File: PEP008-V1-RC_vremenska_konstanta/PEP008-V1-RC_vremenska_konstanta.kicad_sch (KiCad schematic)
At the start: 23 parts, among them J1 Screw_Terminal_01x02

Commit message: 3, 4, 8.
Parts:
- removed D1, D2: LED, LED_SMD:LED_1206_3216Metric_Pad1.42x1.75mm_HandSolder, symbol Device:LED
- removed J1: Screw_Terminal_01x02, TerminalBlock_Phoenix:TerminalBlock_Phoenix_MKDS-1,5-2-5.08_1x02_P5.08mm_Horizontal, symbol Connector:Screw_Terminal_01x02
- removed JP1, JP2, JP3, JP4, JP5, JP6, JP7, JP8: Jumper, Connector_PinHeader_2.54mm:PinHeader_1x02_P2.54mm_Vertical, symbol Jumper:Jumper_2_Bridged
- removed R2: ~, Resistor_SMD:R_1206_3216Metric_Pad1.30x1.75mm_HandSolder, symbol Device:R
- removed R7: 470, Resistor_SMD:R_1206_3216Metric_Pad1.30x1.75mm_HandSolder, symbol Device:R
- removed R8: 4.7k, Resistor_SMD:R_1206_3216Metric_Pad1.30x1.75mm_HandSolder, symbol Device:R
- added C1, C2: 100u, Capacitor_THT:CP_Radial_D8.0mm_P3.50mm, symbol Device:C_Polarized_US
- added J1, J3, J4, J5: Conn_01x01_Pin, Connector_PinHeader_2.54mm:PinHeader_1x01_P2.54mm_Vertical, symbol Connector:Conn_01x01_Pin
- added J2: Screw_Terminal_01x02, TerminalBlock_Phoenix:TerminalBlock_Phoenix_MKDS-1,5-2-5.08_1x02_P5.08mm_Horizontal, symbol Connector:Screw_Terminal_01x02
- added J6, J7: Conn_01x03_Pin, symbol Connector:Conn_01x03_Pin
- added SW1, SW2: SW_SPDT, Button_Switch_THT:SW_E-Switch_EG1224_SPDT_Angled, symbol Switch:SW_SPDT
- R1: value 470 -> 100k
- R3: value 4.7k -> 10k
- R4: value 47k -> 20k
- R5: value 4.7k -> 50k
- R6: value 470 -> 50k
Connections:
- net 0: now also C2.1, J2.2 (Pin_2), J4.1 (Pin_1), SW2.1 (A)
- net at R3.1: now also J7.3 (Pin_3)
- net at R4.1: now also J7.1 (Pin_1); no longer R3.2
- net Output voltage: now reaches R4.2
- net Output voltage: now also R1.2, R3.2, R5.2, R6.2, C1.1, J1.1 (Pin_1)
- net at R5.1: no longer R6.2
- net at R6.1: now also J6.3 (Pin_3)
- net 9V: no longer names the net of R1.1
- net 9V: now also J6.1 (Pin_1)
- new net: J3.1 (Pin_1), J7.2 (Pin_2), SW2.2 (B)
- new net: J5.1 (Pin_1), J6.2 (Pin_2), SW1.1 (A)
- new net: C1.2, C2.2
- new net Input voltage: J2.1 (Pin_1), SW1.2 (B)
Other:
- note added: "Kondenzator"
- note added: "Putanja za pražnjenje"
- note added: "Putanja za punjenje"
- note removed: "Paralelna otpornost"
- note removed: "Redna otpornost"
- title: Redna i paralelna otpornost -> Punjenje i praznjenje kondenzatora
- moved on the sheet: H1, H2, H3, H4

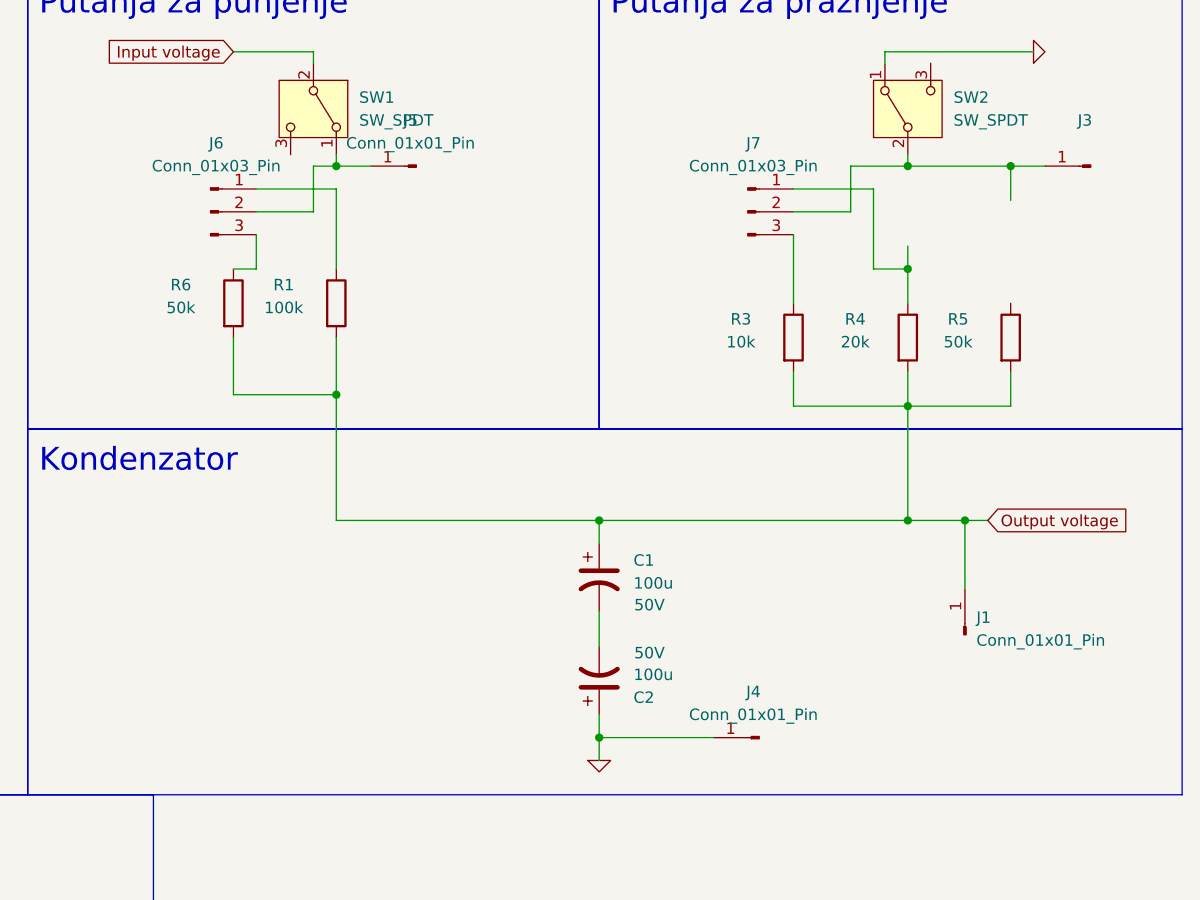
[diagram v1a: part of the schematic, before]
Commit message: PEP006 and PEP009 update.
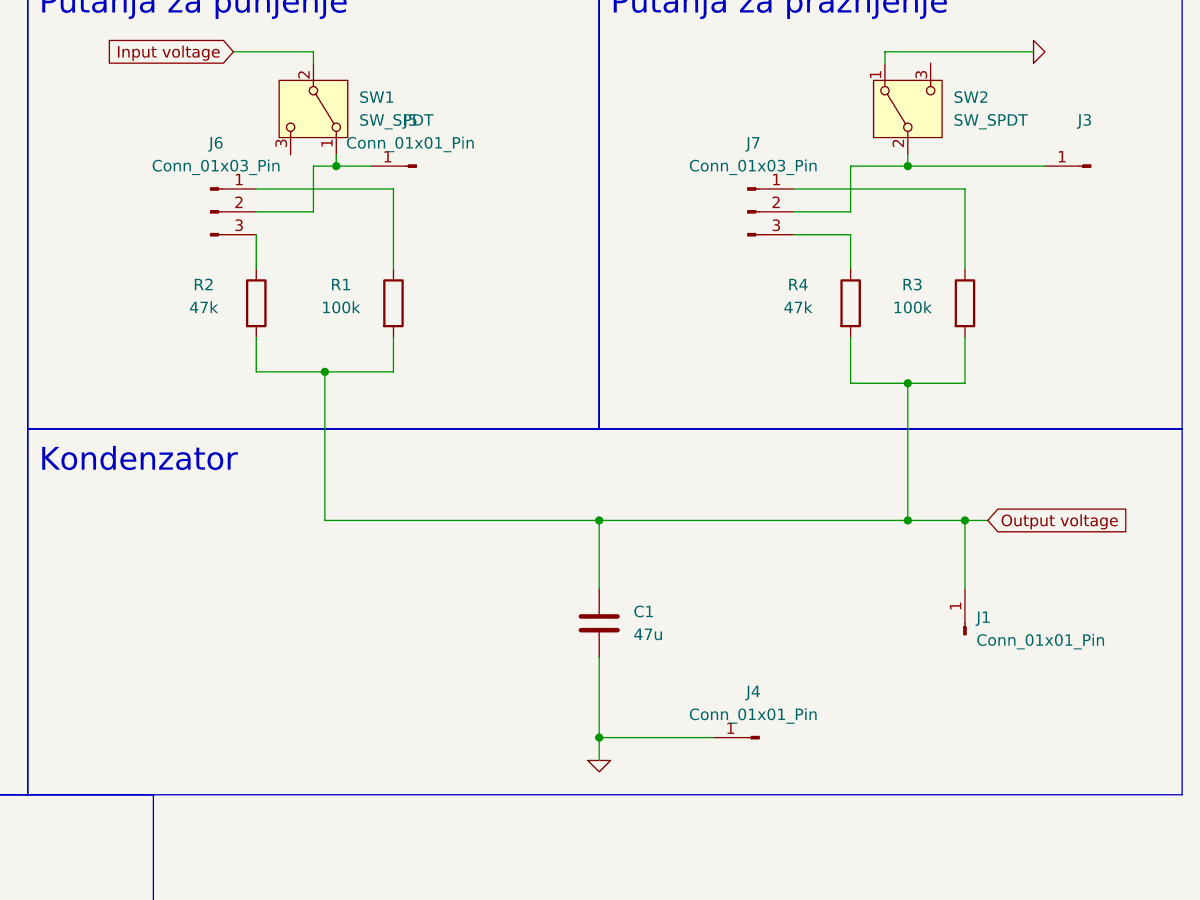
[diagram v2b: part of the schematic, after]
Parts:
- removed C1, C2: 100u, Capacitor_THT:CP_Radial_D8.0mm_P3.50mm, symbol Device:C_Polarized_US
- removed R5: 50k, Resistor_SMD:R_1206_3216Metric_Pad1.30x1.75mm_HandSolder, symbol Device:R
- added C1: 47u, Capacitor_SMD:C_1206_3216Metric, symbol Device:C
- J6, J7: footprint (none) -> Connector_PinHeader_2.54mm:PinHeader_1x03_P2.54mm_Vertical
- R1: LCSC (none) -> C17900
- R2: renamed from R6; value 50k -> 47k; LCSC (none) -> C25664
- R3: renamed from R4; value 20k -> 100k; LCSC (none) -> C17900
- R4: renamed from R3; value 10k -> 47k; LCSC (none) -> C25664
- SW1, SW2: footprint Button_Switch_THT:SW_E-Switch_EG1224_SPDT_Angled -> PEP_library:SW-TH_2MS1T1B1M1QES-5
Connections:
- net 0: now also C1.2
- net Output voltage: now also C1.1
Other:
- moved on the sheet: R1, R2, R3, R4
